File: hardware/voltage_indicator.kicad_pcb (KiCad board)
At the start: 2 copper layers, 45 x 61 mm, 41 parts, among them J1 HV+, J2 HV-, Q1 TK3P80E,RQ, U1 LT8316EFE, U2 LM211DT

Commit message: Improve the layout
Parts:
- removed the G*** at (152.4, 75.1)
- added C9: DNP, Capacitor_SMD:CP_Elec_6.3x5.4, F.Cu at (164.6, 87.8)
- added G***: LOGO, Local_Library:putm_15mm, F.Cu at (154.5, 74.3)
- added R10: 1k2, Resistor_SMD:R_0603_1608Metric, F.Cu at (169.3, 96.7)
- added REF**: Symbol_Highvoltage_Type1_CopperTop_Small, Symbol:Symbol_Highvoltage_Type1_CopperTop_Small, F.Cu at (171.2, 113.0)
- added REF**: Symbol_Highvoltage_Type1_CopperTop_Small, Symbol:Symbol_Highvoltage_Type1_CopperTop_Small, F.Cu at (167.5, 112.9)
- added TP1: LM_N, TestPoint:TestPoint_Pad_D1.0mm, B.Cu at (173.5, 100.8)
- added TP10: LT_VIN, TestPoint:TestPoint_Pad_D1.0mm, B.Cu at (148.1, 106.1)
- added TP11: LT_GATE, TestPoint:TestPoint_Pad_D1.0mm, B.Cu at (150.0, 104.1)
- added TP12: LT_SENSE, TestPoint:TestPoint_Pad_D1.0mm, B.Cu at (160.5, 103.5)
- added TP13: LT_VOUT, TestPoint:TestPoint_Pad_D1.0mm, B.Cu at (166.3, 102.1)
- added TP2: LM_P, TestPoint:TestPoint_Pad_D1.0mm, B.Cu at (170.9, 102.1)
- added TP3: LM_OUT, TestPoint:TestPoint_Pad_D1.0mm, B.Cu at (168.9, 100.8)
- added TP4: LT_D3, TestPoint:TestPoint_Pad_D1.0mm, B.Cu at (152.2, 115.0)
- added TP5: LT_VC, TestPoint:TestPoint_Pad_D1.0mm, B.Cu at (160.4, 108.2)
- added TP6: LT_BIAS, TestPoint:TestPoint_Pad_D1.0mm, B.Cu at (153.7, 110.3)
- added TP7: LT_FB, TestPoint:TestPoint_Pad_D1.0mm, B.Cu at (158.2, 112.0)
- added TP8: LT_GND, TestPoint:TestPoint_Pad_D1.0mm, B.Cu at (162.4, 102.5)
- added TP9: LT_DCM, TestPoint:TestPoint_Pad_D1.0mm, B.Cu at (146.3, 107.3)
- C1: renamed from C3; value 10uF -> 10u
- C2: renamed from C4; value 100nF -> 100n
- C3: renamed from C5; value 100nF -> 100n
- C4: renamed from C1; value 0.1uF -> 100n
- C5: renamed from C2; value 10pF -> 10p
- C6, C7, C8: value 47uF -> 47u
- D1: footprint LED_THT:LED_D5.0mm -> LED_THT:LED_Rectangular_W3.9mm_H1.9mm
- D3: value type="D" model="CMDSH2-3" lib="" -> CMDSH2-3
- D4: value D_Zener 10V -> 10V
- F1: value Fuse 600V -> 600V; footprint vindicator:01020071Z-FUSE-CLIP -> Local_Library:FuseClip
- G***: footprint SignatureBox25mm -> Local_Library:SignatureBox25mm; moved to B.Cu
- J1, J2: footprint Connector_Wire:SolderWire-0.5sqmm_1x01_D0.9mm_OD2.1mm_Relief -> Local_Library:SolderWire_Relief
- L1: value 1mH -> 1m; footprint Inductor_SMD:L_Wuerth_WE-PD2-Typ-MS -> Local_Library:WurthElektronikInductor_7687714102
- Q1: value TK3P80E,RQ -> TK3P80ERQ
- R12: value 21.5kR -> 21k5
- R13: value 2.49kR -> 2k49
- R14: value 22.1kR -> 22k1
- R15: renamed from R11; value 10kR -> 10k
- R16: renamed from R15; value 220mR -> 220m
- R9: renamed from R10; value 240 -> 240R
- moved G*** 49.3 mm to (153.2, 76.2), turned to 180 degrees
- moved J2 29.5 mm to (170.4, 120.6), turned to -90 degrees
- moved R16 9.95 mm to (158.4, 103.7)
- moved D5 8.70 mm to (163.7, 100.1)
- moved J1 5.83 mm to (138.6, 120.6)
- moved R11 5.13 mm to (169.3, 95.1)
- moved C6 4.56 mm to (163.6, 97.7)
- moved C7 4.46 mm to (163.6, 95.1)
- moved C8 4.46 mm to (163.6, 92.6)
- moved D1 4.25 mm to (172.0, 92.9)
- moved REF** 4.12 mm to (174.0, 74.0)
- moved C4 4.05 mm to (150.7, 86.8)
- moved REF** 4.00 mm to (174.0, 126.0)
- moved U1 4.00 mm to (170.4, 101.2)
- moved R7 3.82 mm to (174.9, 85.2), turned to 180 degrees
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- renumbered R5 to R11, R6 to R5, R7 to R6, R8 to R7, R9 to R8, U2 to U1, U1 to U2
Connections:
- D3 pad 1: Net-(D2-K) -> Net-(D3-K)
- D3 pad 2: Net-(D3-K) -> Net-(D2-K)
- F1 pad 1: +VDC -> VCC
- F1 pad 2: Net-(F1-Pad2) -> Net-(J1-Pin_1)
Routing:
- net +VDC: track 57.5 -> 0.00 mm
- net VCC: track 0.00 -> 56.6 mm
- net Net-(D5-K): track 57.3 -> 27.0 mm, vias 2 -> 1
- net Net-(F1-Pad2): track 16.2 -> 0.00 mm
- net Net-(J1-Pin_1): track 0.00 -> 12.4 mm
- net GND: track 42.0 -> 52.8 mm, vias 14 -> 48
- net Net-(Q1-S): track 14.0 -> 20.8 mm, vias 0 -> 1
- net +12V: track 42.5 -> 38.2 mm, vias 2 -> 3
- net Net-(Q1-G): track 16.7 -> 20.5 mm, vias 0 -> 2
- net Net-(U2-DCM): track 2.65 -> 6.04 mm, vias 0 -> 1
- net Net-(U1-+): track 3.62 -> 6.36 mm, vias 0 -> 1
- net Net-(D1-K): track 6.53 -> 9.13 mm, vias 0 -> 1
- net Net-(U2-VC): track 2.60 -> 4.86 mm, vias 0 -> 1
- net Net-(D2-K): track 4.81 -> 6.11 mm, vias 0 -> 1
- net Net-(U1--): track 32.5 -> 31.3 mm, vias 2 -> 1
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- added copper zone on F.Cu, net Net-(D3-K)
- added copper zone on F.Cu, net Net-(D4-A)
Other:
- board size 45 x 61 mm -> 49 x 62 mm
- board text added: "+"
- board text added: "-"
- board text added: "Hleb Fedarovich"
- board text added: "Jakub Drankiewicz"
- board text added: "Rev: 2.0"

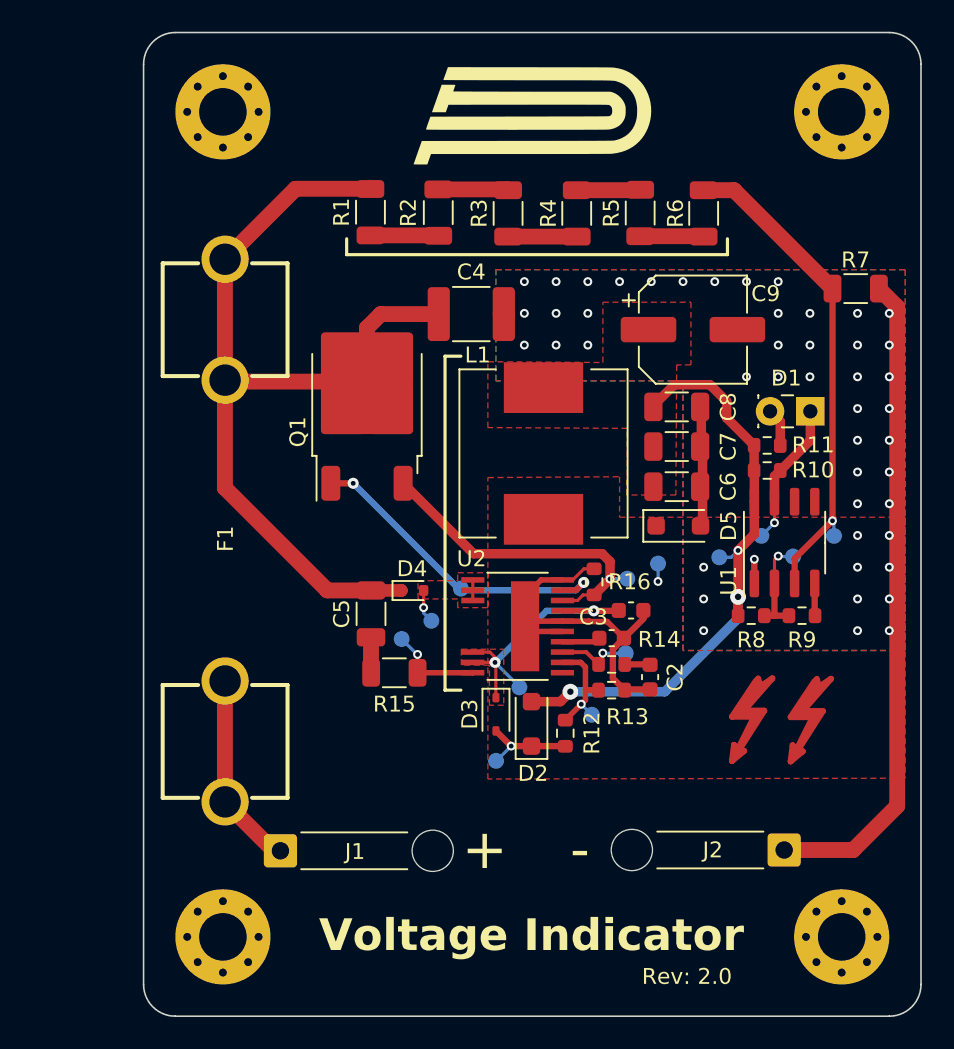
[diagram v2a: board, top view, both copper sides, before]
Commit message: Use a transistor to drive the LED
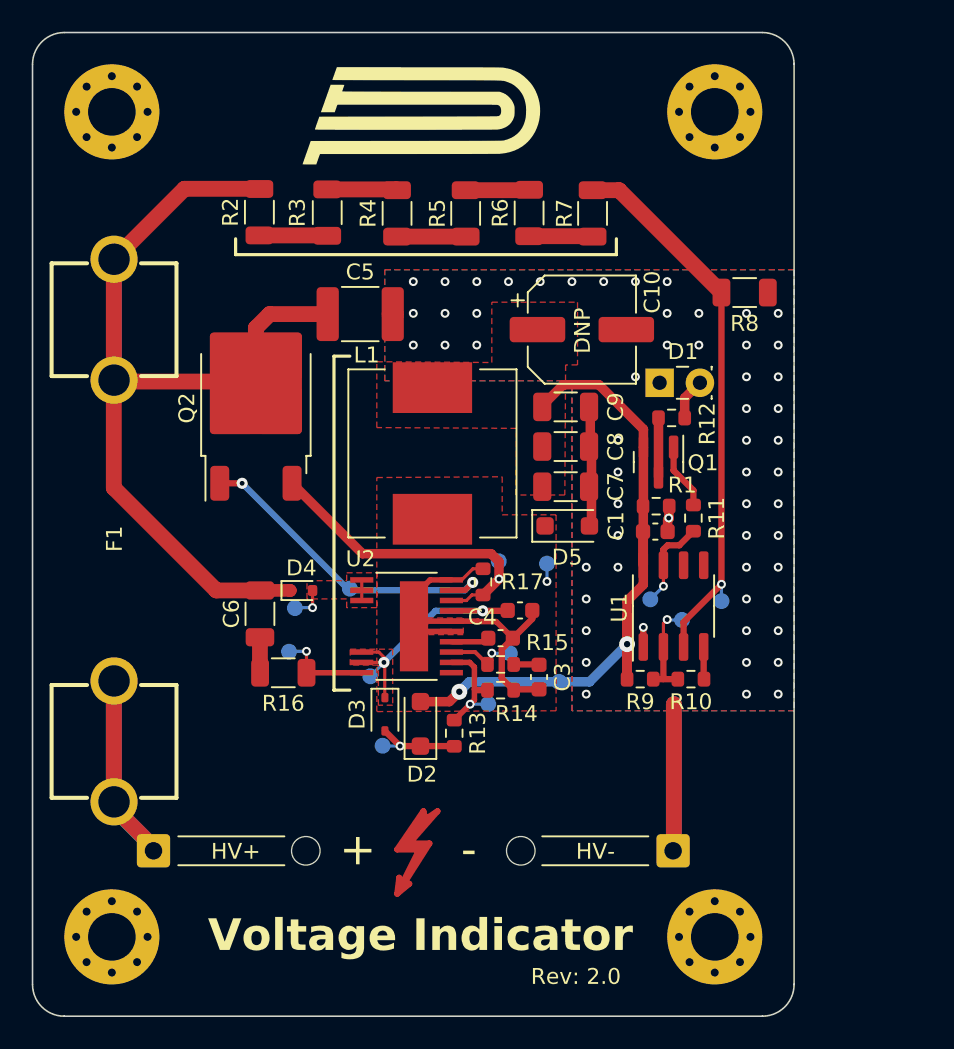
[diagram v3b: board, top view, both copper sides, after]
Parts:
- removed the REF** at (171.2, 113.0)
- removed the REF** at (167.5, 112.9)
- added C1: 100n, Capacitor_SMD:C_0603_1608Metric, F.Cu at (162.3, 100.5)
- added Q1: BC807, Package_TO_SOT_SMD:SOT-23, F.Cu at (162.5, 96.1)
- added R12: TBD, Resistor_SMD:R_0603_1608Metric, F.Cu at (163.3, 93.3)
- added REF**: Symbol_Highvoltage_Type1_CopperTop_Small, Local_Library:HighVoltageSmall, F.Cu at (146.4, 121.3)
- R11: value 143R -> TBD
- moved TP13 12.8 mm to (156.2, 110.0)
- moved D1 9.67 mm to (162.5, 91.1), turned to 0 degrees
- moved TP6 9.43 mm to (144.3, 109.6)
- moved TP10 8.64 mm to (139.5, 105.3)
- moved TP1 8.20 mm to (166.4, 104.9)
- moved TP12 8.17 mm to (152.4, 102.4)
- moved R10 8.06 mm to (164.5, 109.8)
- moved R9 8.06 mm to (161.3, 109.8)
- moved TP2 8.06 mm to (163.9, 106.1)
- moved TP3 8.06 mm to (161.9, 104.8)
- moved U1 8.06 mm to (163.4, 105.2)
- moved J1 8.00 mm to (130.6, 120.6)
- moved REF** 8.00 mm to (166.0, 126.0)
- moved REF** 8.00 mm to (166.0, 74.0)
- moved R1 7.35 mm to (162.3, 98.9)
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- renumbered C9 to C10, C1 to C2, C2 to C3, C3 to C4, C4 to C5, C5 to C6, C6 to C7, C7 to C8, C8 to C9, Q1 to Q2, R10 to R1, R9 to R10, R12 to R13, R13 to R14, R14 to R15, R15 to R16, R16 to R17, R1 to R2, R2 to R3, R3 to R4, R4 to R5, R5 to R6, R6 to R7, R7 to R8, R8 to R9
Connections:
- D1 pad 1: Net-(D1-K) -> GND
- R1 pad 2: Net-(D1-K) -> GND
- R11 pad 1: +12V -> Net-(R11-Pad1)
- R11 pad 2: Net-(D1-A) -> Net-(Q1-B)
- TP3 pad 1: Net-(D1-K) -> Net-(R11-Pad1)
- U1 pad 7: Net-(D1-K) -> Net-(R11-Pad1)
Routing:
- net GND: track 52.8 -> 31.2 mm, vias 48 -> 58
- net Net-(J1-Pin_1): track 12.4 -> 23.5 mm
- net Net-(D1-K): track 9.13 -> 0.00 mm, vias 1 -> 0
- net VCC: track 56.6 -> 64.2 mm
- net +12V: track 38.2 -> 45.0 mm, vias 3 -> 2
- net Net-(R11-Pad1): track 0.00 -> 5.85 mm, vias 0 -> 1
- net Net-(Q1-B): track 0.00 -> 4.16 mm
- net Net-(U1--): track 31.3 -> 35.2 mm
- net Net-(Q1-C): track 0.00 -> 3.72 mm
- net Net-(D3-K): track 18.9 -> 17.9 mm
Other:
- board size 49 x 62 mm -> 48 x 62 mm
- board text added: "DNP"
- board text added: "HV+"
- board text added: "HV-"

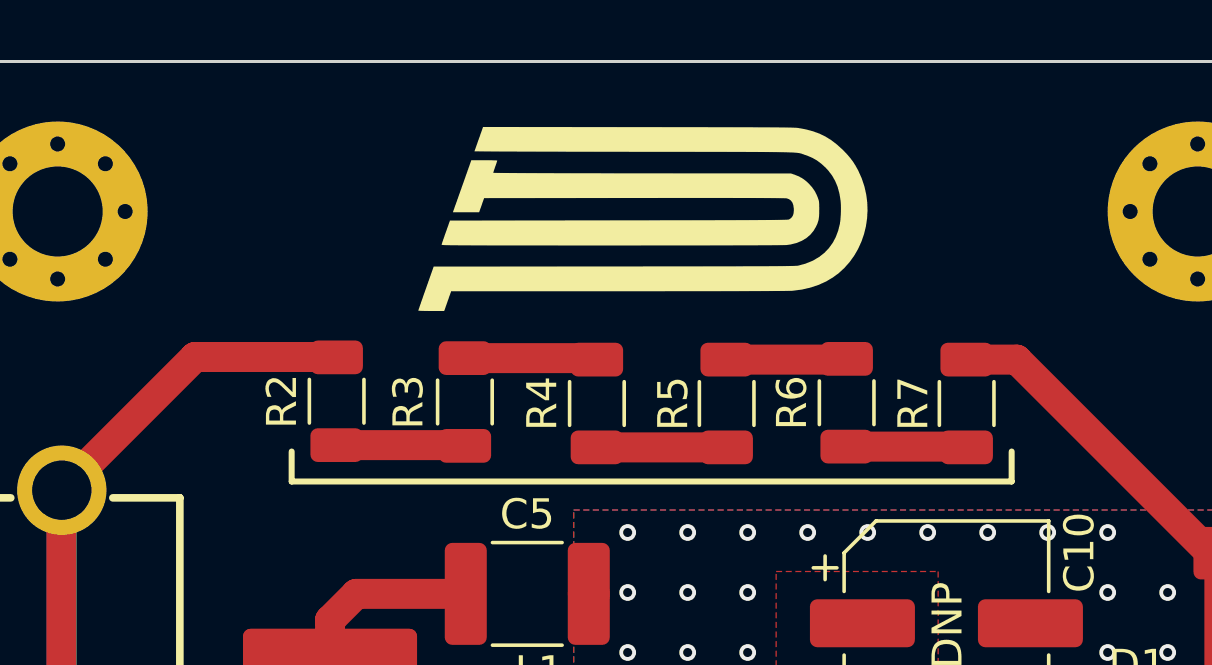
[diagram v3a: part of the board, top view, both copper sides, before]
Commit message: Align the signature box
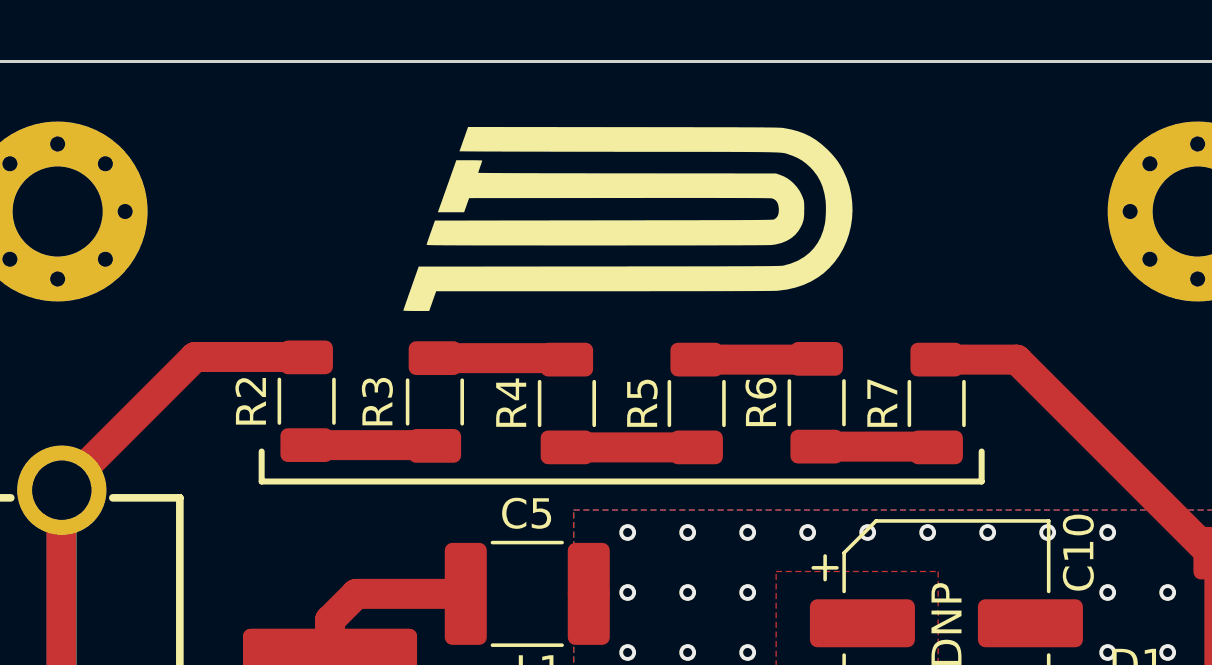
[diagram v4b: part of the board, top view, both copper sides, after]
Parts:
- moved R2 1.00 mm to (136.3, 80.4)
- moved R3 1.00 mm to (140.6, 80.4)
- moved R4 1.00 mm to (145.0, 80.5)
- moved R5 1.00 mm to (149.3, 80.5)
- moved R6 1.00 mm to (153.3, 80.4)
- moved R7 1.00 mm to (157.3, 80.5)
- moved G*** 0.50 mm to (147.0, 74.3)
- moved G*** 0.50 mm to (145.7, 76.2)
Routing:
- net Net-(U1--): track 35.2 -> 36.2 mm
- net VCC: track 64.2 -> 63.2 mm
